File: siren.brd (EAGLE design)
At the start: 33 x 33 mm, 11 parts

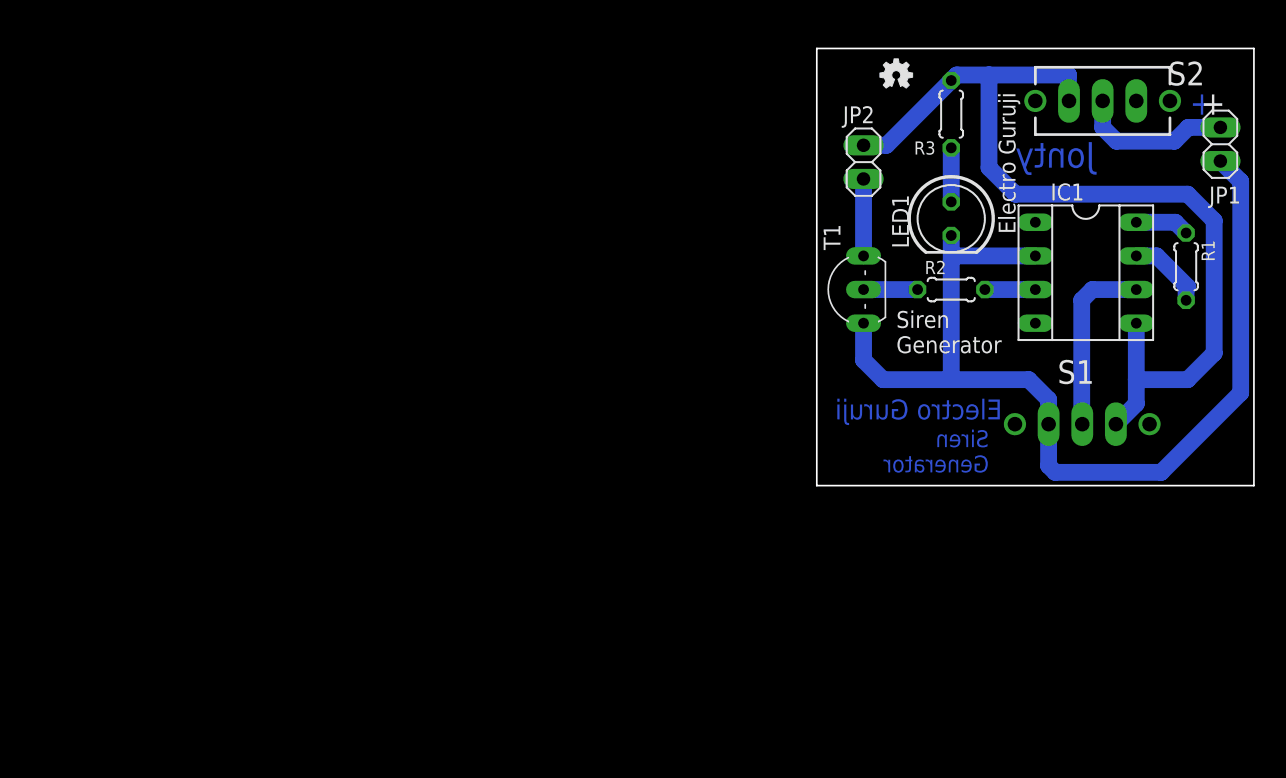
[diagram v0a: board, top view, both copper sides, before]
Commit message: SP3T replaced with 5 header pins
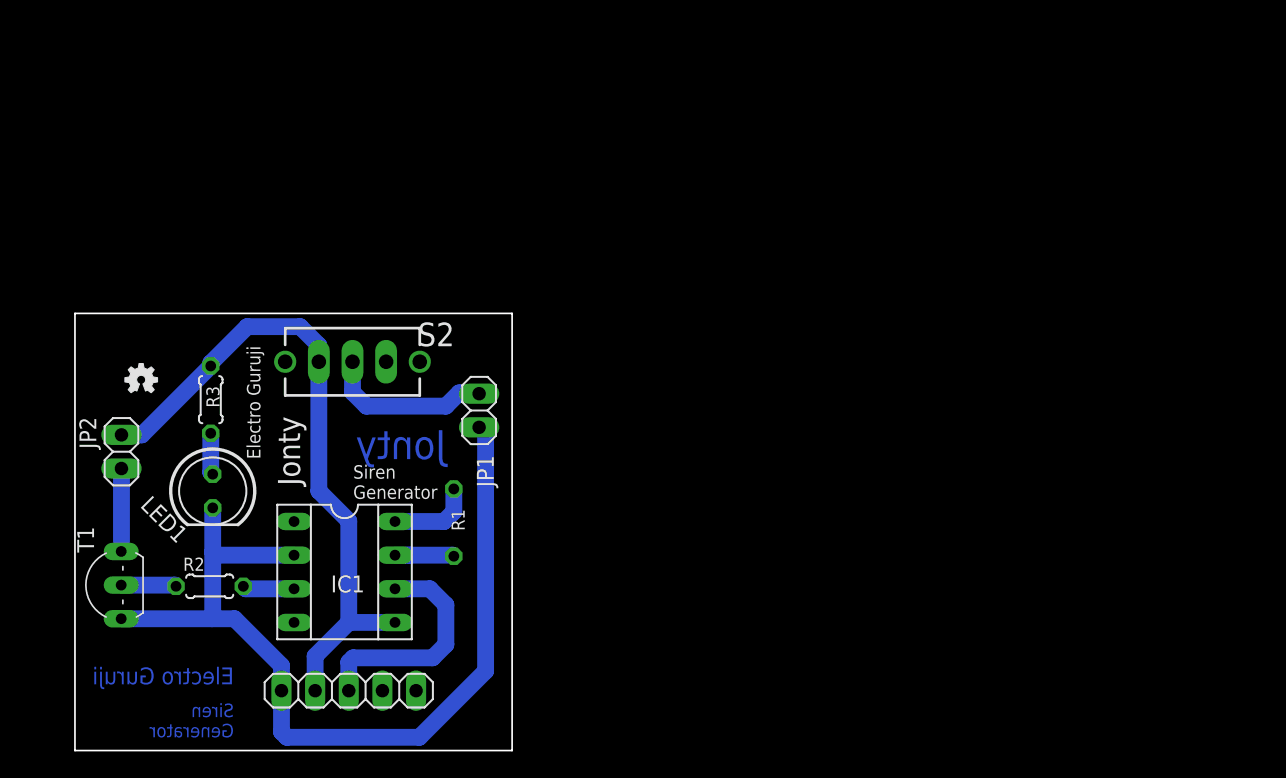
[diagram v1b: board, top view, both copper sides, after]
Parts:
- removed S1: TL39YO, switch:TL3XYO
- added JP3: SP3T, pinhead:1X05
- IC1: value (none) -> UM3561
- JP1: value (none) -> 3V Supply
- JP2: value (none) -> Speaker
- T1: value (none) -> BC547
- moved U$1 61.5 mm to (39.0, 44.0)
- moved IC1 60.3 mm to (54.4, 29.5)
- moved T1 60.3 mm to (36.2, 28.5)
- moved R2 60.3 mm to (44.2, 28.4)
- moved JP2 60.1 mm to (37.5, 38.6)
- moved S2 60.0 mm to (55.0, 45.4)
- moved R3 59.9 mm to (44.2, 42.5)
- moved JP1 59.5 mm to (64.5, 41.7)
- moved LED1 59.4 mm to (44.4, 35.6)
- moved R1 58.6 mm to (62.6, 33.2), flipped to the bottom
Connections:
- net GND: now also JP3.5; no longer S1.1
- net SEL1: now also JP3.3; no longer S1.2
- net VDD: now also JP3.4; no longer S1.3
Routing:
- net VDD: track 70.3 -> 50.5 mm
- net GND: track 75.7 -> 69.5 mm
- net SEL1: track 13.8 -> 17.4 mm
- net OSC2: track 4.10 -> 6.47 mm
- net N$1: track 11.8 -> 12.7 mm
- net N$2: track 4.08 -> 3.15 mm
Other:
- board text removed: "+"
